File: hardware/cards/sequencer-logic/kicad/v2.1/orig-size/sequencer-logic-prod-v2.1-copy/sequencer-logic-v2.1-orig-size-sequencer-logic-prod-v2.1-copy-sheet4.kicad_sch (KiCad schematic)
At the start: 10 parts, among them IC12 74*08, IC24 74*32, IC25 74*374, IC26 74*374, IC27 74*374, IC28 74*374, IC29 74*08, IC30 74*04, IC35 74*32, IC36 74*04

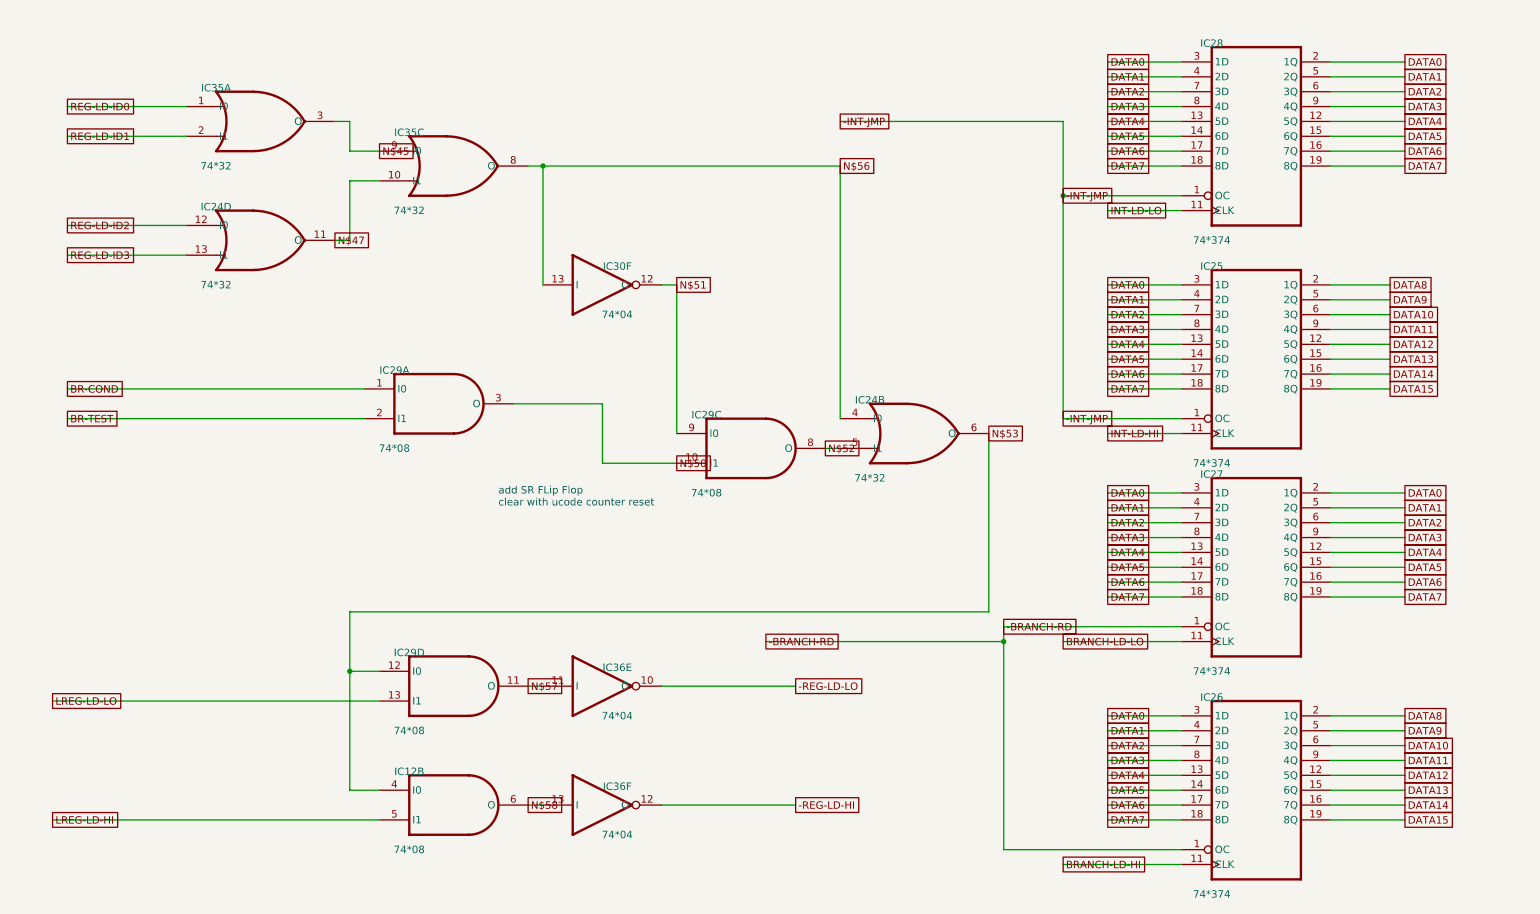
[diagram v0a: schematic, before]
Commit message: fix(kicad): readable converted schematics - overlaps 42,847 -> 3,147, nothing off the frame; CF sheet 0 overlaps
- tools/kicad/sch_overlaps.py: calibrated readability check (text/text, text/body, text/line, off frame/title block)
- eagle_sch_to_kicad.py: fields placed from Eagle's smashed attributes or the symbol's >NAME/>VALUE with Eagle's align,
  size and ratio, readable angles; fields Eagle never shows hidden (FABC96R shows only its pin name); pin numbers hidden
  where every Eagle pin hides them; Eagle-hidden layers dropped (the stray SpiceOrder text); labels on their own wires,
  converter labels only where KiCad needs them; rotate-then-mirror fixed for MR90/MR270 in pin_world/no-connects;
  each sheet on the smallest page that holds it, centred clear of the title block
- finish_board.py: stable footprint-library choice (DRC counts no longer vary run to run)
- all 37 projects regenerated: netlist proofs unchanged (34 MATCH, 2 schematic-only, video Fusion export MISMATCH as
  before); DRC same or better; ERC up (loose wire ends onto graphic buses no longer hidden by labels; explained per README)
- CF card: gate names off the gate bodies, U3 clear of its title, 5.08 mm connector pins; rebuilt: DRC 0/0, proof MATCH
- schematic PDFs regenerated (tools/sch_to_pdf.py, 37/37)

Co-Authored-By: Claude Opus 5.5 <noreply@anthropic.com>
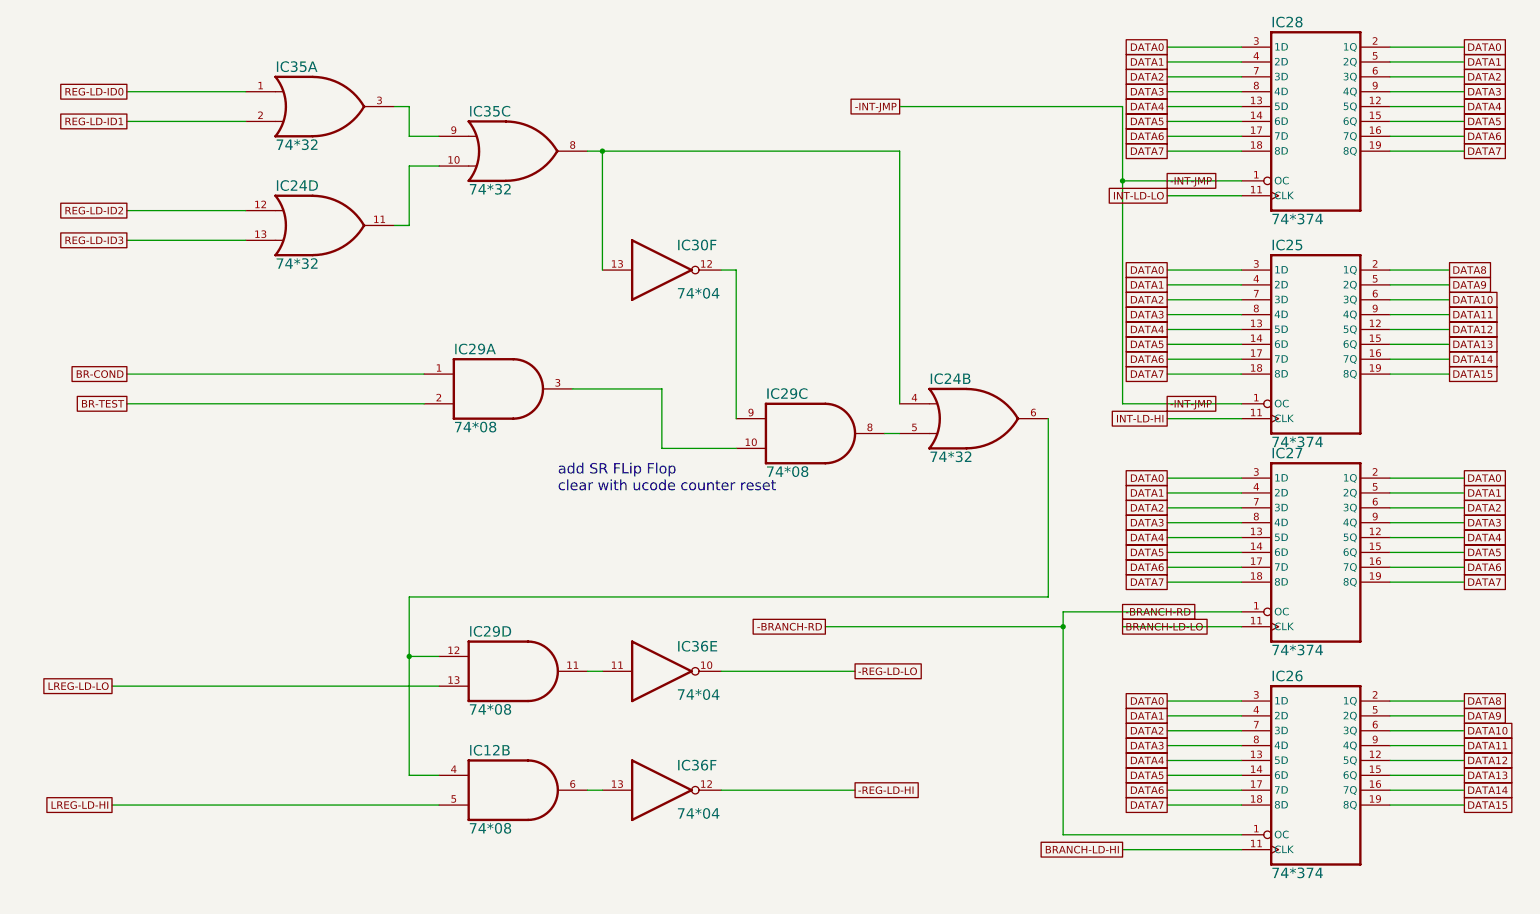
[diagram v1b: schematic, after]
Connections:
- net N$45: no longer names the net of IC35.3 (O), IC35.9 (I0)
- net N$47: no longer names the net of IC24.11 (O), IC35.10 (I1)
- net N$50: no longer names the net of IC29.10 (I1), IC29.3 (O)
- net N$51: no longer names the net of IC29.9 (I0), IC30.12 (O)
- net N$52: no longer names the net of IC24.5 (I1), IC29.8 (O)
- net N$53: no longer names the net of IC12.4 (I0), IC24.6 (O), IC29.12 (I0)
- net N$56: no longer names the net of IC24.4 (I0), IC30.13 (I), IC35.8 (O)
- net N$57: no longer names the net of IC29.11 (O), IC36.11 (I)
- net N$58: no longer names the net of IC12.6 (O), IC36.13 (I)
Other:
- moved on the sheet: IC25, IC26, IC27, IC28
